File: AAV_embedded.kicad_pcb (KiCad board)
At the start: 4 copper layers, 168.2 x 114.7 mm, 83 parts, among them J1 JTAG_SWD_CONN, J10 DRV_HIGH_C2, J11 DRV_LOW_C2, J12 DRV_HIGH_C3, J13 DRV_LOW_C3, J14 DRV_LOW_C1, J15 Brake/FwRev, J16 5v_in, J17 3.3v_in, J18 12v_in, J2 Raspberry_Pi_4, J21 CAN, J23 5v_rail, J24 3.3v_rail, J25 12v_rail, J26 GND_rail, J27 12v_rail_f, J28 3.3v_rail_f, J29 5v_rail_f, J3 USB_C_Receptacle_USB2.0_14P, J30 GND_rail_f, J5 THR_EN_JMP, J6 Conn_01x07, J7 Conn_01x05, J8 Throttle Connector, J9 DRV_HIGH_C1, SW1 DAC_ADDR, SW2 IO_EXT_ADDR, SW3 SW_DIP_x03, SW4 5v_USB_EN, SW5 THR_EN, SW6 ~{RESET_uMOD}, SW7 ~{BOOT_uMOD}, SW8 ~{RESET_BRK}, SW9 ~{RESET_STR}, U1 DAC101C081CIMK, U2 PCA9555D, U3 74AHC1G08, U5 FXMA108, U6 MCP2515-xSO, U7 SN65HVD230, Y1 16MHz

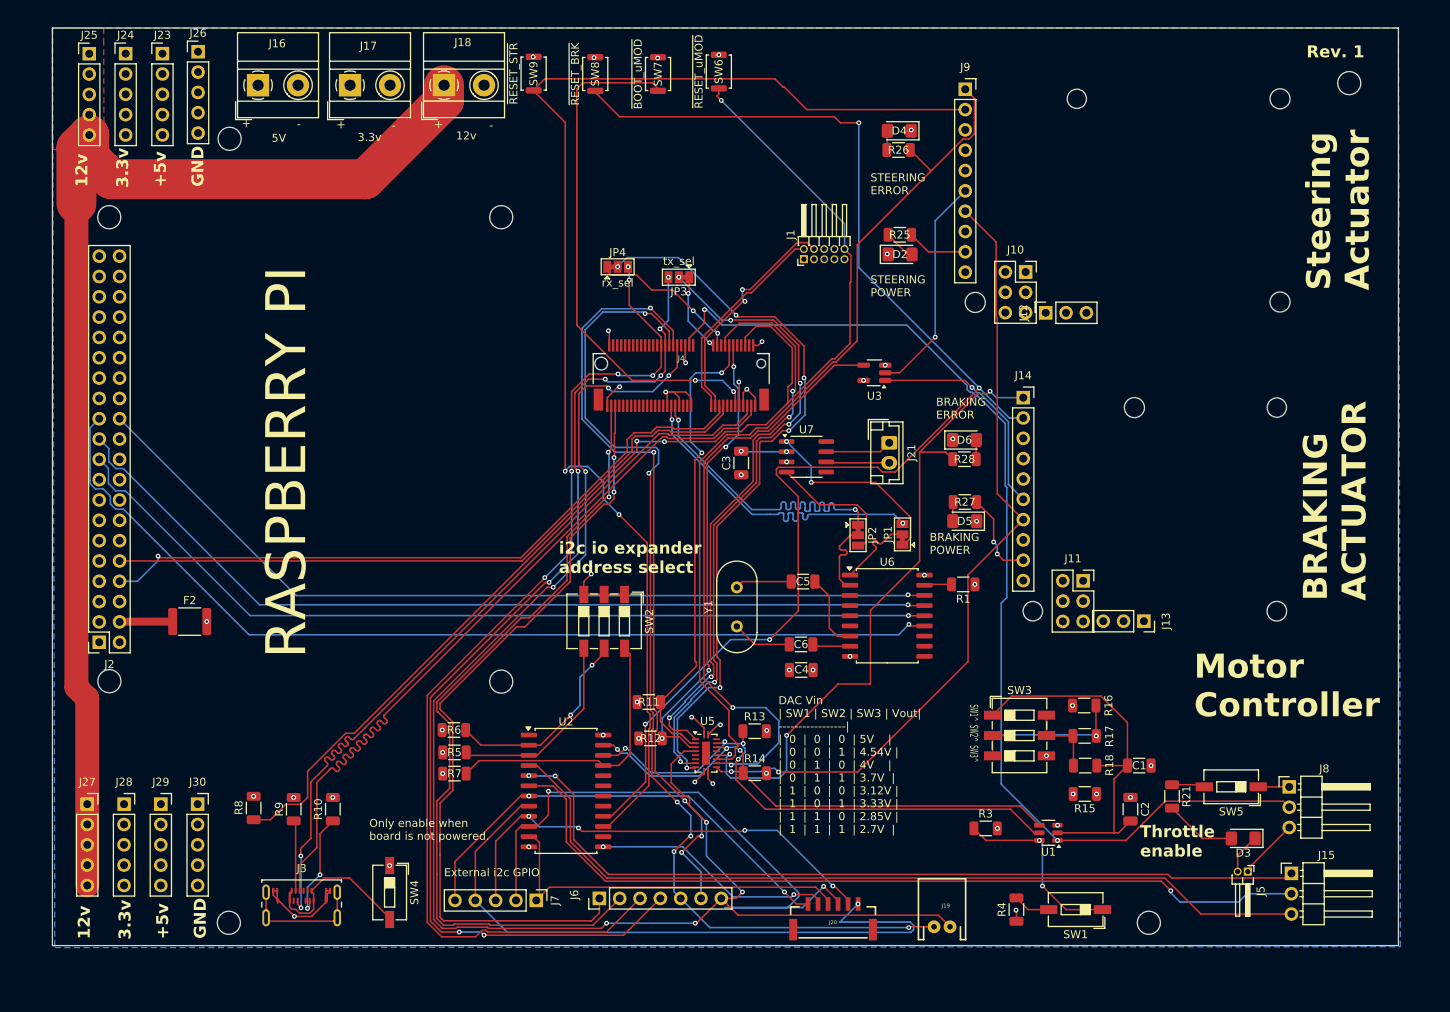
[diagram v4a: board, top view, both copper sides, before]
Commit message: i2c address fix and logo
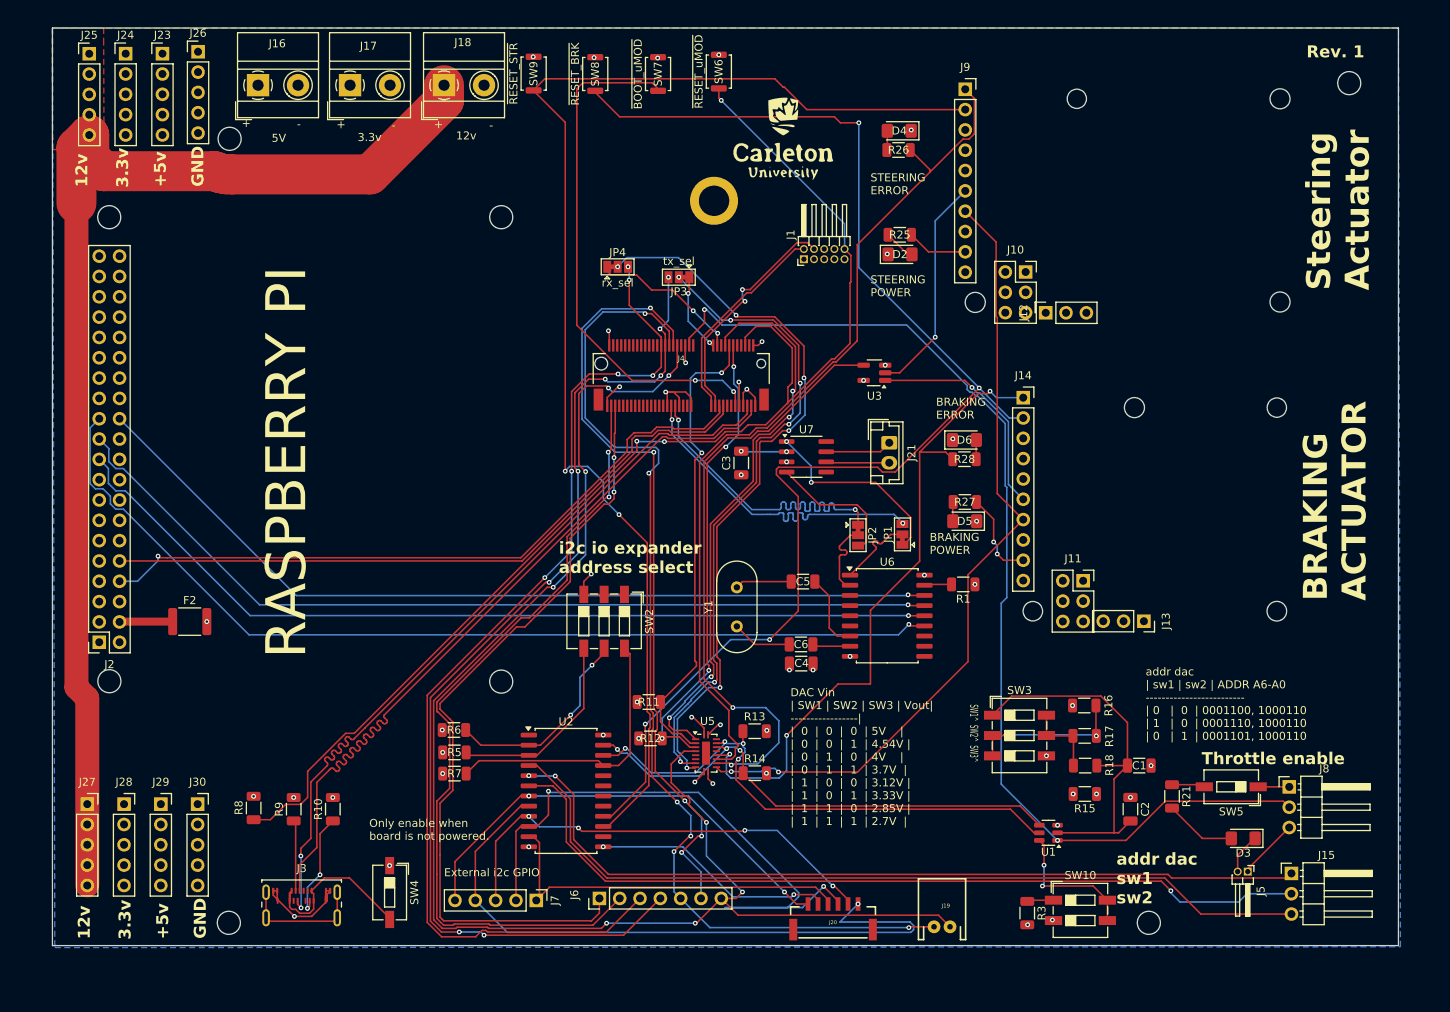
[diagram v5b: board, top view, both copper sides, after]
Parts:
- removed R4: 10k, Resistor_SMD:R_1206_3216Metric
- removed SW1: DAC_ADDR, Button_Switch_SMD:SW_DIP_SPSTx01_Slide_6.7x4.1mm_W6.73mm_P2.54mm_LowProfile_JPin
- added ?: , SparkFun-Hardware:STAND-OFF-REFLOW-M2.5, F.Cu at (130.7, 64.8)
- added G***: LOGO, LOGO, F.Cu at (139.3, 57.0)
- added SW10: SW_DIP_x02, Button_Switch_SMD:SW_DIP_SPSTx02_Slide_6.7x6.64mm_W6.73mm_P2.54mm_LowProfile_JPin, F.Cu at (176.4, 153.4)
- moved R3 11.8 mm to (169.8, 153.8), turned to -90 degrees
- moved C4 0.80 mm to (141.6, 122.6)
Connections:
- R3 pad 1: Net-(U1-ADR0) -> Net-(R3-Pad1)
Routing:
- net Net-(U1-ADR0): track 23.4 -> 17.4 mm
- net Net-(R4-Pad2): track 4.64 -> 0.00 mm
- net Net-(R3-Pad1): track 0.00 -> 3.35 mm
- net GND: track 52.2 -> 51.0 mm
- net +12V: track 150.5 -> 149.9 mm
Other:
- board text added: "addr dac sw1 sw2"
- board text added: "addr dac | sw1 | sw2 | ADDR A6-A0 ------------------------- | 0 | 0 | 0001100, 1000110 | 1 | 0 | 0001110, 1000110 | 0 | 1 | 0001101, 1000110"
- board text removed: "Motor Controller"

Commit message: fix dac
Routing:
- net ~{RESET_uMOD}: track 156.4 -> 155.5 mm
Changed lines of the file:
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@@
 	)
 	(gr_text "Steering\nActuator"
-		(at 212.85 75.95 90)
+		(at 213.3 75.25 90)
 		(layer "F.SilkS")
 		(effects
@@
 	)
 	(segment
-		(start 131.25 51.9)
-		(end 131.55 52.2)
-		(width 0.2)
-		(layer "F.Cu")
-		(net 142)
-	)
-	(segment
 		(start 134.05 93.6)
 		(end 132.068628 93.6)
@@
 	)
 	(segment
-		(start 131.25 50.7)
-		(end 131.25 51.9)
-		(width 0.2)
-		(layer "F.Cu")
-		(net 142)
-	)
-	(segment
 		(start 145.368628 84.5)
 		(end 139.759314 90.109314)
@@
 		(width 0.2)
 		(layer "F.Cu")
+		(net 142)
+	)
+	(segment
+		(start 131.25 50.7)
+		(end 131.25 51.4)
+		(width 0.2)
+		(layer "F.Cu")
